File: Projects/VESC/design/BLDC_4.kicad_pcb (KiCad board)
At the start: 4 copper layers, 38.5 x 65 mm, 127 parts, among them K1 SERVO, P1 HALL/Encoder, P101 CANBUS, P2 SWD, P3 PWR_COMM, P4 IN+, P5 IN-, P6 MOTOR1, P7 MOTOR2, P9 MOTOR3, Q1 IRFS7530, Q2 IRFS7530, Q3 IRFS7530, Q4 IRFS7530, Q5 IRFS7530, Q6 IRFS7530, U1 STM32F40X_LQFP64, U2 TC2117, U3 DRV8302, U401 SN65HVD232, X1 MINI-USB-SHIELD-32005-201, X2 8MHz 10ppm

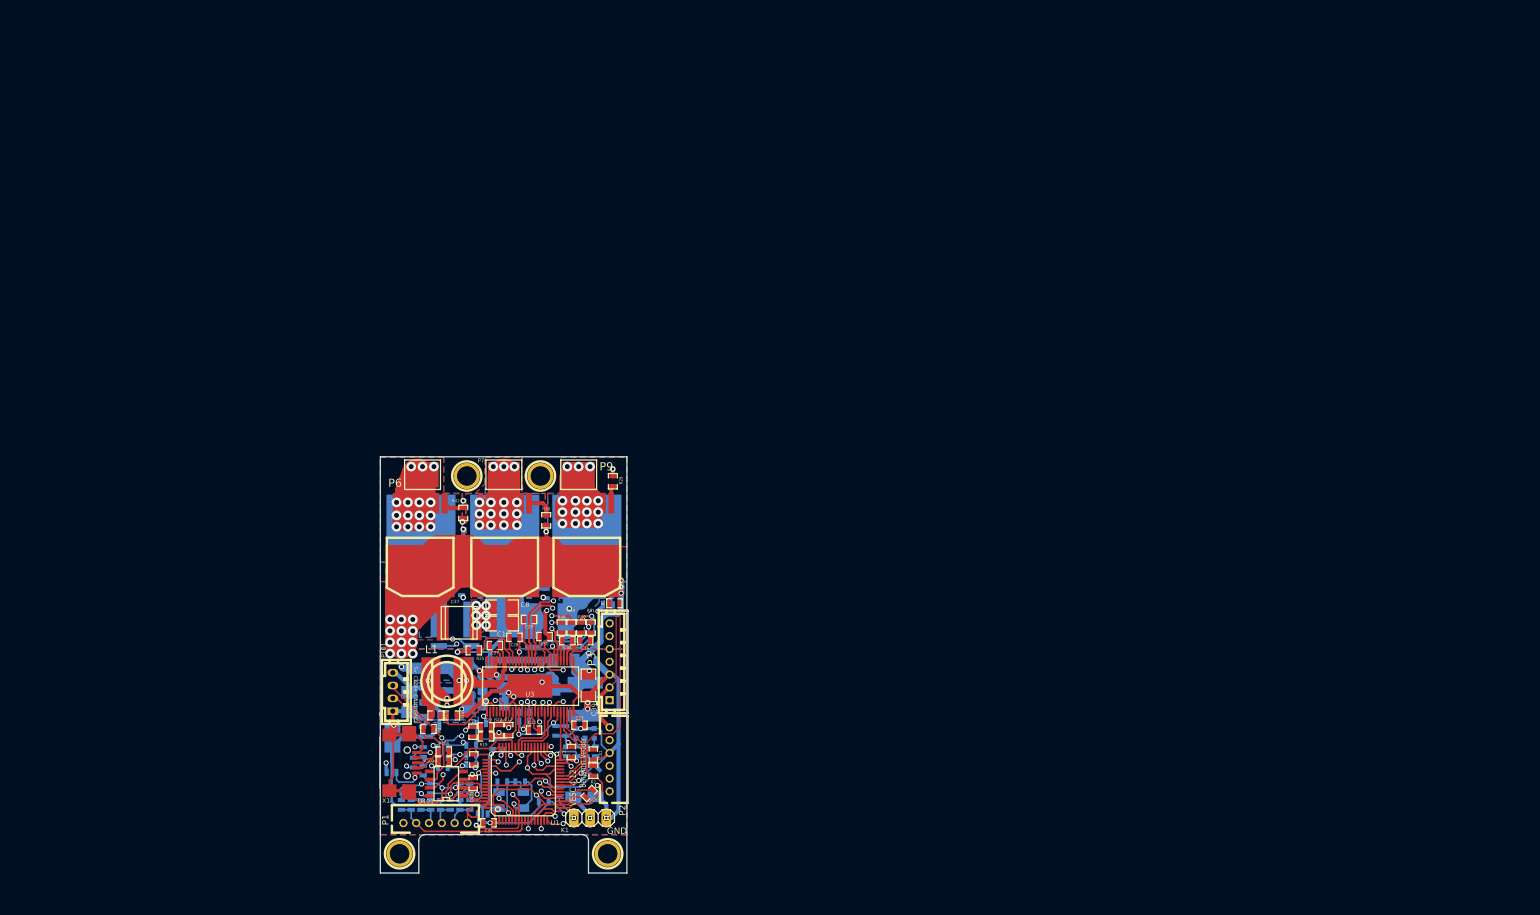
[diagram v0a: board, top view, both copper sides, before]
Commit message: Started making changes to VESC layout and schematic
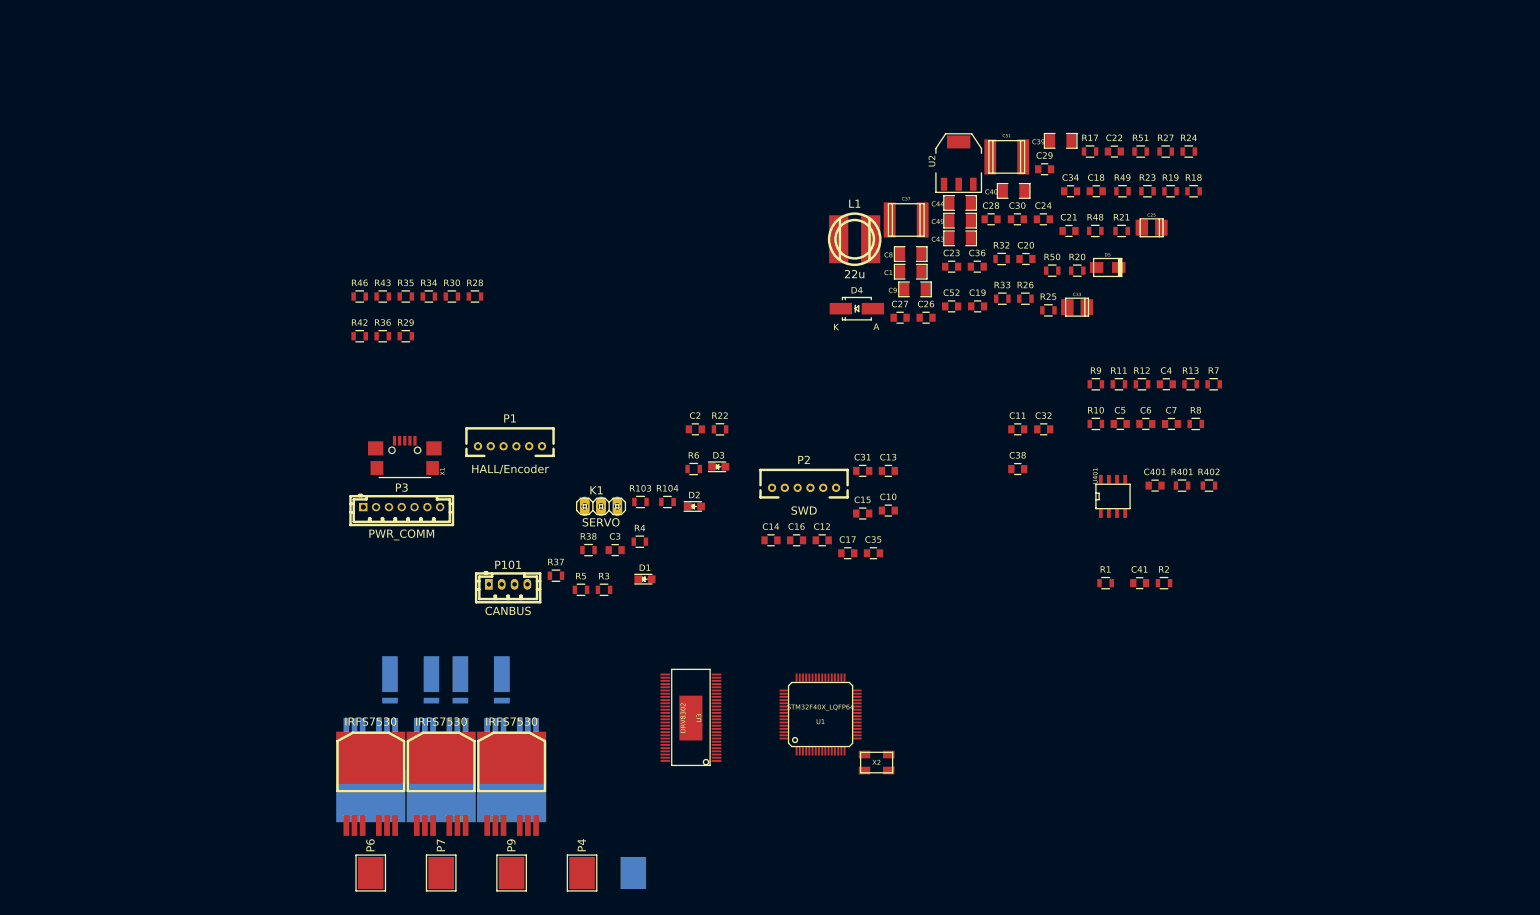
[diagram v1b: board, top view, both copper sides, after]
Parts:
- removed 1PIN (x2): P***, 1pin
- removed 1PIN (x2): P***, Connect:1pin
- removed G***: oshw_silkscreen-back_3mm, oshw_silkscreen-back_3mm
- C10, C11, C12, C13, C19, C21, C22, C23, C27, C28, C29, C30, C34, C35, C36, C401, C41: footprint CRF1:SMD-0603_c -> Capacitors_SMD:C_0805
- C14, C15, C16, C17, C18, C2, C20, C24, C26, C3, C31, C32, C38, C4, C5, C52, C6, C7: footprint CRF1:SMD-0603_c -> Capacitors_SMD:C_0805; moved to F.Cu
- C25, C33, C40, C43, C44, C49, C51, C9, D4, D5, P4, U2: moved to F.Cu
- D1, D2, D3: footprint LEDs:LED-0603 -> LEDs:LED_0805; moved to F.Cu
- R1, R103, R104, R17, R18, R19, R2, R20, R25, R28, R34, R401, R42, R48, R49, R50, R51: footprint CRF1:SMD-0603_r -> Resistors_SMD:R_0805
- R10, R11, R12, R13, R21, R22, R23, R24, R26, R27, R29, R3, R30, R32, R33, R35, R36, R37, R38, R4, R402, R43, R46, R5, R6, R7, R8, R9: footprint CRF1:SMD-0603_r -> Resistors_SMD:R_0805; moved to F.Cu
- X2: value 8MHz 10ppm -> CRYSTAL_GROUND_PIN; moved to F.Cu
- moved R24 147.4 mm to (204.7, 32.3), turned to 0 degrees
- moved R27 143.7 mm to (201.1, 32.3), turned to 0 degrees
- moved C25 142.7 mm to (198.9, 44.2), turned to 0 degrees
- moved R23 142.2 mm to (198.3, 38.5)
- moved R18 141.8 mm to (205.5, 38.5)
- moved R7 141.5 mm to (208.6, 68.7), turned to 0 degrees
- moved R13 137.0 mm to (205.0, 68.7), turned to 0 degrees
- moved R19 136.7 mm to (201.9, 38.5)
- moved C4 136.3 mm to (201.2, 68.7), turned to 0 degrees
- moved R17 134.9 mm to (189.3, 32.3)
- moved R402 134.2 mm to (207.9, 84.5), turned to 0 degrees
- moved R8 133.5 mm to (205.8, 74.9), turned to 0 degrees
- moved C7 128.9 mm to (202.0, 74.9), turned to 0 degrees
- moved C22 128.0 mm to (193.1, 32.3)
- moved R12 127.7 mm to (197.4, 68.7), turned to 0 degrees
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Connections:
- net /MCU/MISO_ADC_EXT2 renamed /MISO_RX_SCL
- net /MCU/RX_SCL_MOSI renamed /RX_SCL_MOSI
- net /MCU/SCK_ADC_EXT renamed /SCK_ADC_EXT
- net /MCU/TX_SDA_NSS renamed /TX_SDA
- P2 pad 6: Net-(P2-Pad6) -> (no net)
- U1 pad 11: Net-(U1-Pad11) -> (no net)
- U1 pad 2: Net-(U1-Pad2) -> (no net)
- U1 pad 28: Net-(U1-Pad28) -> (no net)
- U1 pad 3: Net-(U1-Pad3) -> (no net)
- U1 pad 39: Net-(U1-Pad39) -> (no net)
- U1 pad 4: Net-(U1-Pad4) -> (no net)
- U1 pad 40: Net-(U1-Pad40) -> (no net)
- U1 pad 50: Net-(U1-Pad50) -> (no net)
- U1 pad 54: Net-(U1-Pad54) -> (no net)
- U1 pad 55: Net-(U1-Pad55) -> (no net)
- U1 pad 56: Net-(U1-Pad56) -> (no net)
- U1 pad 9: Net-(U1-Pad9) -> (no net)
- U3 pad 4: Net-(U3-Pad4) -> (no net)
- U3 pad 5: Net-(U3-Pad5) -> (no net)
- U3 pad 55: Net-(U3-Pad55) -> (no net)
- U3 pad 56: Net-(U3-Pad56) -> (no net)
- U401 pad 5: Net-(U401-Pad5) -> (no net)
- X1 pad 4: Net-(X1-Pad4) -> (no net)
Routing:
- net GND: track 398.8 -> 0.00 mm, vias 27 -> 0
- net V_SUPPLY: track 290.3 -> 0.00 mm, vias 20 -> 0
- net VCC: track 185.2 -> 0.00 mm, vias 9 -> 0
- net /Mosfet driver/H3_VS: track 166.9 -> 0.00 mm, vias 18 -> 0
- net /Mosfet driver/H1_VS: track 150.6 -> 0.00 mm, vias 17 -> 0
- net /Mosfet driver/H2_VS: track 145.0 -> 0.00 mm, vias 17 -> 0
- net +5V: track 115.3 -> 0.00 mm, vias 4 -> 0
- net /Mosfet driver/H3_LOW: track 53.5 -> 0.00 mm, vias 2 -> 0
- net /Mosfet driver/M_H1: track 49.8 -> 0.00 mm, vias 2 -> 0
- net /Mosfet driver/H1_LOW: track 48.5 -> 0.00 mm, vias 2 -> 0
- net /TX_SDA: track 47.1 -> 0.00 mm, vias 2 -> 0
- net /MCU/ADC_TEMP: track 44.0 -> 0.00 mm
- net /RX_SCL_MOSI: track 41.6 -> 0.00 mm, vias 1 -> 0
- net /Mosfet driver/M_H3: track 40.9 -> 0.00 mm, vias 2 -> 0
- net /MISO_RX_SCL: track 36.0 -> 0.00 mm, vias 1 -> 0
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- removed copper zone on B.Cu, net /Mosfet driver/H1_LOW
- removed copper zone on B.Cu, net /Mosfet driver/H1_VS
- removed copper zone on F.Cu, net /Mosfet driver/H1_VS
- removed copper zone on GND, net /Mosfet driver/H1_VS
- removed copper zone on GND2, net /Mosfet driver/H1_VS
- removed copper zone on B.Cu, net /Mosfet driver/H2_VS
- removed copper zone on F.Cu, net /Mosfet driver/H2_VS
- removed copper zone on GND, net /Mosfet driver/H2_VS
- removed copper zone on GND2, net /Mosfet driver/H2_VS
- removed copper zone on B.Cu, net /Mosfet driver/H3_LOW
- removed copper zone on B.Cu, net /Mosfet driver/H3_VS
- removed copper zone on F.Cu, net /Mosfet driver/H3_VS
- removed copper zone on GND, net /Mosfet driver/H3_VS
- removed copper zone on GND2, net /Mosfet driver/H3_VS
- removed copper zone on B.Cu, net GND
- removed copper zone on F.Cu, net GND
- removed copper zone on GND, net GND
- removed copper zone on GND2, net GND
- removed copper zone on B.Cu, net VCC
- removed copper zone on F.Cu, net V_SUPPLY
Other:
- board outline removed
- board text removed: "3.3V"
- board text removed: "3.3v"
- board text removed: "5v"
- board text removed: "ADC"
- board text removed: "ADC2"
- board text removed: "Benjamin Vedder"
- board text removed: "CANH"
- board text removed: "CANL"
- board text removed: "CLK"
- board text removed: "DIO"
- board text removed: "GND"
- board text removed: "H1"
- board text removed: "H2"
- board text removed: "H3"
- board text removed: "MISO"
- board text removed: "MOSI"
- board text removed: "NSS"
- board text removed: "RST"
- board text removed: "RX"
- board text removed: "SCK"
- board text removed: "SCL"
- board text removed: "SDA"
- board text removed: "TEMP"
- board text removed: "TX"
- board text removed: "VESC 4.12"
- board text removed: "vedder.se"

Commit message: More schematic updates for VESC
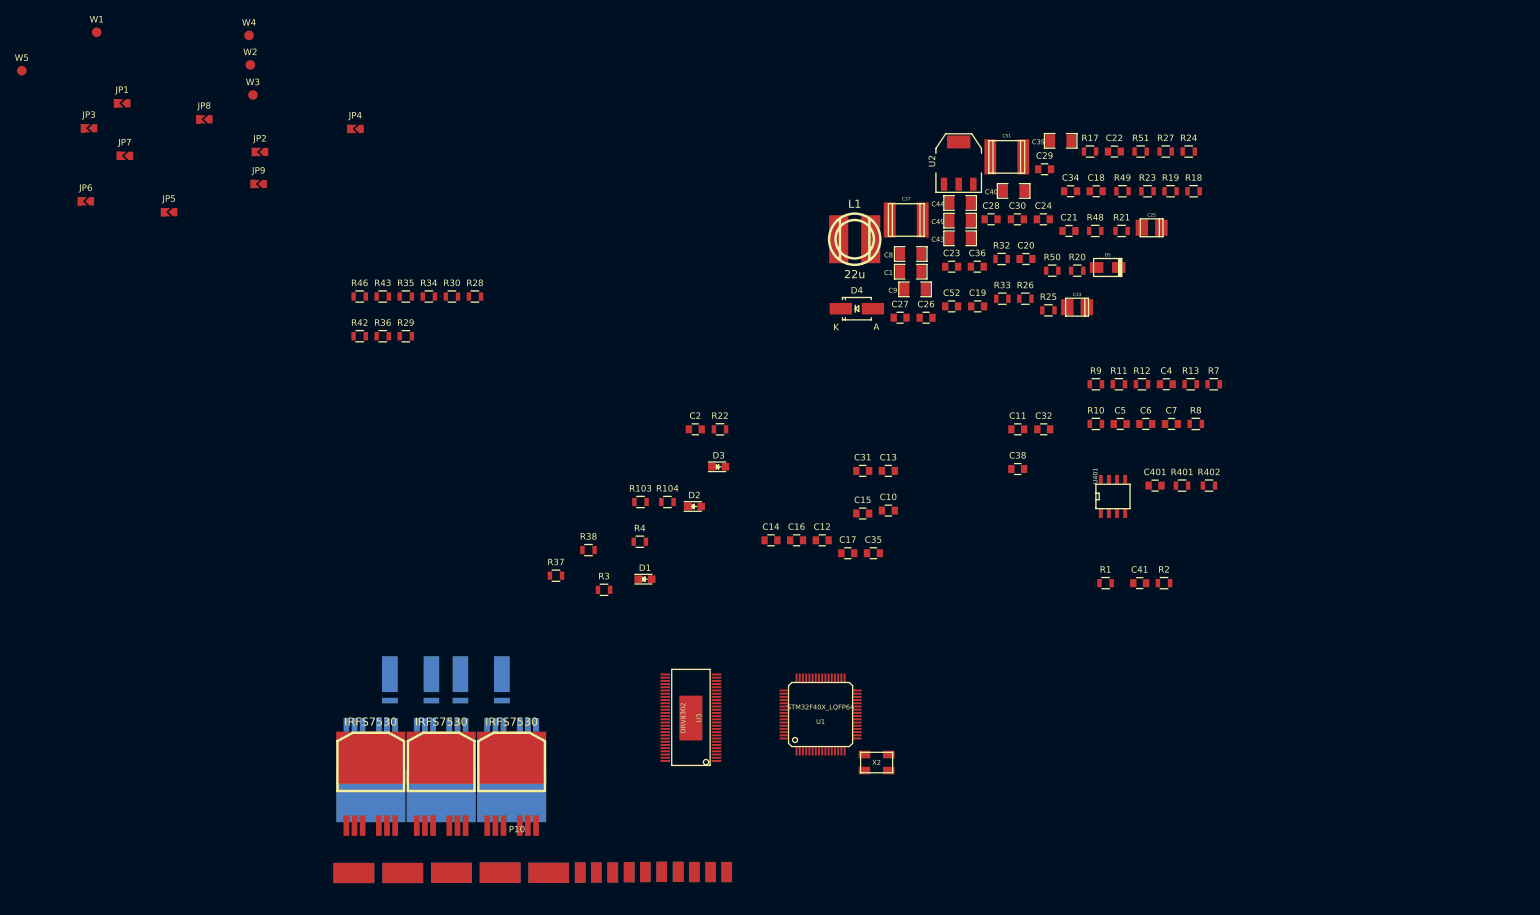
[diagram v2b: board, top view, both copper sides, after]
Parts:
- removed C3: 100n, Capacitors_SMD:C_0805
- removed K1: SERVO, CRF1:pinhead-1X03
- removed P1: HALL/Encoder, CRF1:MICRO_JST_6
- removed P101: CANBUS, JST conn:b4b-ph-kl
- removed P2: SWD, CRF1:MICRO_JST_6
- removed P3: PWR_COMM, CRF1:b7b-ph-kl
- removed P4: IN+, CRF1:1PAD_4x5mm
- removed P5: IN-, CRF1:1PAD_4x5mm
- removed P6: MOTOR1, CRF1:1PAD_4x5mm
- removed P7: MOTOR2, CRF1:1PAD_4x5mm
- removed P9: MOTOR3, CRF1:1PAD_4x5mm
- removed R5: 2k2, Resistors_SMD:R_0805
- removed R6: 0R, Resistors_SMD:R_0805
- removed X1: MINI-USB-SHIELD-32005-201, CRF1:USB-UX60R-MB-5ST
- added JP1: Jumper_NC_Small, USST-footprints:J_0805, F.Cu at (38.2, 24.8)
- added JP2: Jumper_NC_Small, USST-footprints:J_0805, F.Cu at (59.7, 32.4)
- added JP3: Jumper_NC_Small, USST-footprints:J_0805, F.Cu at (33.0, 28.7)
- added JP4: Jumper_NC_Small, USST-footprints:J_0805, F.Cu at (74.6, 28.8)
- added JP5: Jumper_NC_Small, USST-footprints:J_0805, F.Cu at (45.5, 41.8)
- added JP6: Jumper_NC_Small, USST-footprints:J_0805, F.Cu at (32.5, 40.1)
- added JP7: Jumper_NC_Small, USST-footprints:J_0805, F.Cu at (38.6, 33.0)
- added JP8: Jumper_NC_Small, USST-footprints:J_0805, F.Cu at (51.0, 27.3)
- added JP9: Jumper_NC_Small, USST-footprints:J_0805, F.Cu at (59.5, 37.4)
- added P10: AMP17614426-2_EDGE, USST-footprints:TE2007088-1_Edge, F.Cu at (99.8, 148.5)
- added W1: SWD_VCC, Measurement_Points:Measurement_Point_Round-SMD-Pad_Small, F.Cu at (34.2, 13.7)
- added W2: SWCLK, Measurement_Points:Measurement_Point_Round-SMD-Pad_Small, F.Cu at (58.2, 18.8)
- added W3: SWDIO, Measurement_Points:Measurement_Point_Round-SMD-Pad_Small, F.Cu at (58.6, 23.5)
- added W4: NRST, Measurement_Points:Measurement_Point_Round-SMD-Pad_Small, F.Cu at (58.0, 14.2)
- added W5: SWD_GND, Measurement_Points:Measurement_Point_Round-SMD-Pad_Small, F.Cu at (22.5, 19.7)
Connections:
- net /Filters/HALL1_IN renamed /CardEdge/H1
- net /Filters/HALL2_IN renamed /CardEdge/H2
- net /Filters/HALL3_IN renamed /CardEdge/H3
- net /RX_SCL_MOSI renamed /MCU/RX_SCL_MOSI
- net /TX_SDA renamed /MCU/TX_SDA_NSS
- D1 pad 1: Net-(D1-Pad1) -> GND
- D1 pad 2: GND -> Net-(D1-Pad2)
- D2 pad 1: Net-(D2-Pad1) -> GND
- D2 pad 2: GND -> Net-(D2-Pad2)
- D3 pad 1: Net-(D3-Pad1) -> GND
- D3 pad 2: GND -> Net-(D3-Pad2)
- R103 pad 2: Net-(R103-Pad2) -> /CardEdge/USB_DM
- R104 pad 2: Net-(R104-Pad2) -> /CardEdge/USB_DP
- R22 pad 1: Net-(D3-Pad1) -> Net-(D3-Pad2)
- R37 pad 1: Net-(D1-Pad1) -> Net-(D1-Pad2)
- R38 pad 1: Net-(D2-Pad1) -> Net-(D2-Pad2)
- U1 pad 11: (no net) -> Net-(U1-Pad11)
- U1 pad 2: (no net) -> Net-(U1-Pad2)
- U1 pad 21: /SCK_ADC_EXT -> /MCU/SCK_ADC_EXT
- U1 pad 22: /MISO_RX_SCL -> /MCU/MISO_ADC_EXT2
- U1 pad 28: (no net) -> Net-(U1-Pad28)
- U1 pad 3: (no net) -> Net-(U1-Pad3)
- U1 pad 39: (no net) -> Net-(U1-Pad39)
- U1 pad 4: (no net) -> Net-(U1-Pad4)
- U1 pad 40: (no net) -> Net-(U1-Pad40)
- U1 pad 50: (no net) -> Net-(U1-Pad50)
- U1 pad 52: /Filters/HALL3_OUT -> /MCU/HALL_3
- U1 pad 54: (no net) -> Net-(U1-Pad54)
- U1 pad 55: (no net) -> Net-(U1-Pad55)
- U1 pad 56: (no net) -> Net-(U1-Pad56)
- U1 pad 58: /Filters/HALL1_OUT -> /CardEdge/CS
- U1 pad 59: /Filters/HALL2_OUT -> /MCU/HALL_2
- U1 pad 9: (no net) -> Net-(U1-Pad9)
- U3 pad 4: (no net) -> Net-(U3-Pad4)
- U3 pad 5: (no net) -> Net-(U3-Pad5)
- U3 pad 55: (no net) -> Net-(U3-Pad55)
- U3 pad 56: (no net) -> Net-(U3-Pad56)
- U401 pad 5: (no net) -> Net-(U401-Pad5)
